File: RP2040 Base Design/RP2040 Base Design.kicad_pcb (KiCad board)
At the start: 2 copper layers, 75 x 23 mm, 27 parts, among them J1 USB_B_Micro, J2 Conn_01x02, J3 RP2040_SWD, U1 RP2040, U2 AMS1117-3.3, U3 W25Q128JVS, Y1 X322512MSB4SI

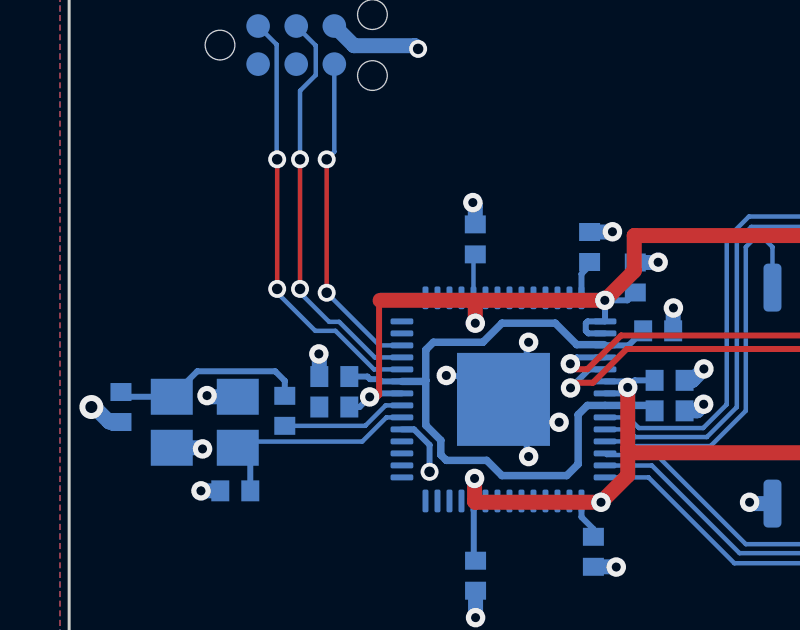
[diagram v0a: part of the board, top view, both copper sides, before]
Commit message: Add 10k pullup resistor to RUN pin for debugging Fixes #2
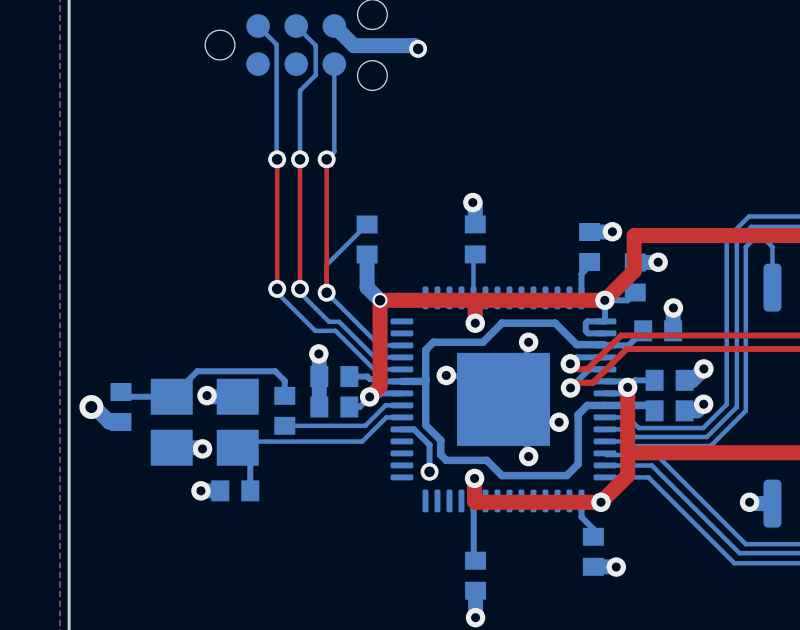
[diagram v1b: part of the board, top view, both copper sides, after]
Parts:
- added R6: 10k, Custom_Footprints:Perfect_0402, B.Cu at (27.0, 26.8)
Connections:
- net /GPIO00 renamed /RP2040/GPIO00
- net /GPIO01 renamed /RP2040/GPIO01
- net /GPIO02 renamed /RP2040/GPIO02
- net /GPIO03 renamed /RP2040/GPIO03
- net /GPIO04 renamed /RP2040/GPIO04
- net /GPIO05 renamed /RP2040/GPIO05
- net /GPIO06 renamed /RP2040/GPIO06
- net /GPIO07 renamed /RP2040/GPIO07
- net /GPIO08 renamed /RP2040/GPIO08
- net /GPIO09 renamed /RP2040/GPIO09
- net /GPIO10 renamed /RP2040/GPIO10
- net /GPIO11 renamed /RP2040/GPIO11
- net /GPIO12 renamed /RP2040/GPIO12
- net /GPIO13 renamed /RP2040/GPIO13
- net /GPIO14 renamed /RP2040/GPIO14
- net /GPIO15 renamed /RP2040/GPIO15
- net /GPIO16 renamed /RP2040/GPIO16
- net /GPIO17 renamed /RP2040/GPIO17
- net /GPIO18 renamed /RP2040/GPIO18
- net /GPIO19 renamed /RP2040/GPIO19
- net /GPIO20 renamed /RP2040/GPIO20
- net /GPIO21 renamed /RP2040/GPIO21
- net /GPIO22 renamed /RP2040/GPIO22
- net /GPIO23 renamed /RP2040/GPIO23
- net /GPIO24 renamed /RP2040/GPIO24
- net /GPIO25 renamed /RP2040/GPIO25
- net /GPIO26 renamed /RP2040/GPIO26
- net /GPIO27 renamed /RP2040/GPIO27
- net /GPIO28 renamed /RP2040/GPIO28
- net /GPIO29 renamed /RP2040/GPIO29
- net /QSPI_SCLK renamed /RP2040/QSPI_SCLK
- net /QSPI_SD0 renamed /RP2040/QSPI_SD0
- net /QSPI_SD1 renamed /RP2040/QSPI_SD1
- net /QSPI_SD2 renamed /RP2040/QSPI_SD2
- net /QSPI_SD3 renamed /RP2040/QSPI_SD3
- net /QSPI_SS renamed /RP2040/QSPI_SS
- net /SWCLK renamed /RP2040/SWCLK
- net /SWD renamed /RP2040/SWD
- net /USB_D+ renamed /RP2040/USB_D+
- net /USB_D- renamed /RP2040/USB_D-
- net /USB_D_R+ renamed /RP2040/USB_D_R+
- net /USB_D_R- renamed /RP2040/USB_D_R-
- net /XIN renamed /RP2040/XIN
- net /XOUT renamed /RP2040/XOUT
- net /XOUT_R renamed /RP2040/XOUT_R
- net /~{RST} renamed /RP2040/~{RST}
- net /~{USB_BOOT} renamed /RP2040/~{USB_BOOT}
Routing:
- net /RP2040/~{RST}: track 11.0 -> 13.8 mm
- net +3V3: track 73.7 -> 75.5 mm, vias 8 -> 9
- net GND: track 25.9 -> 26.9 mm

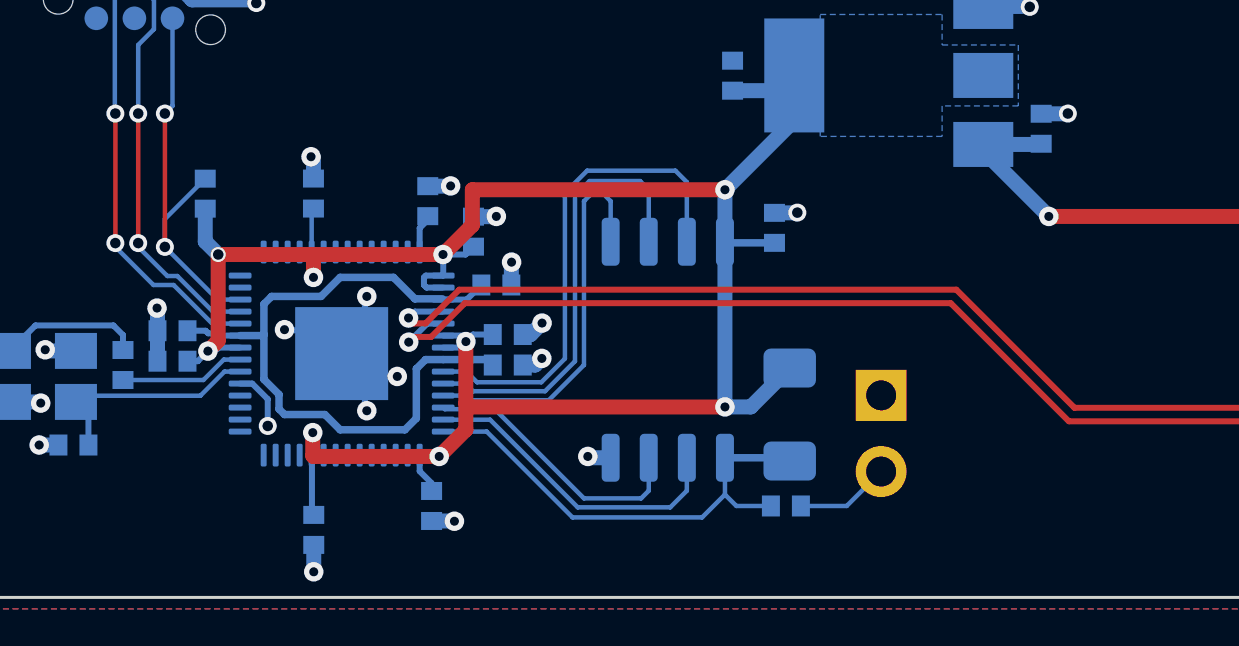
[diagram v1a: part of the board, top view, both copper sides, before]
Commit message: Add default sizes
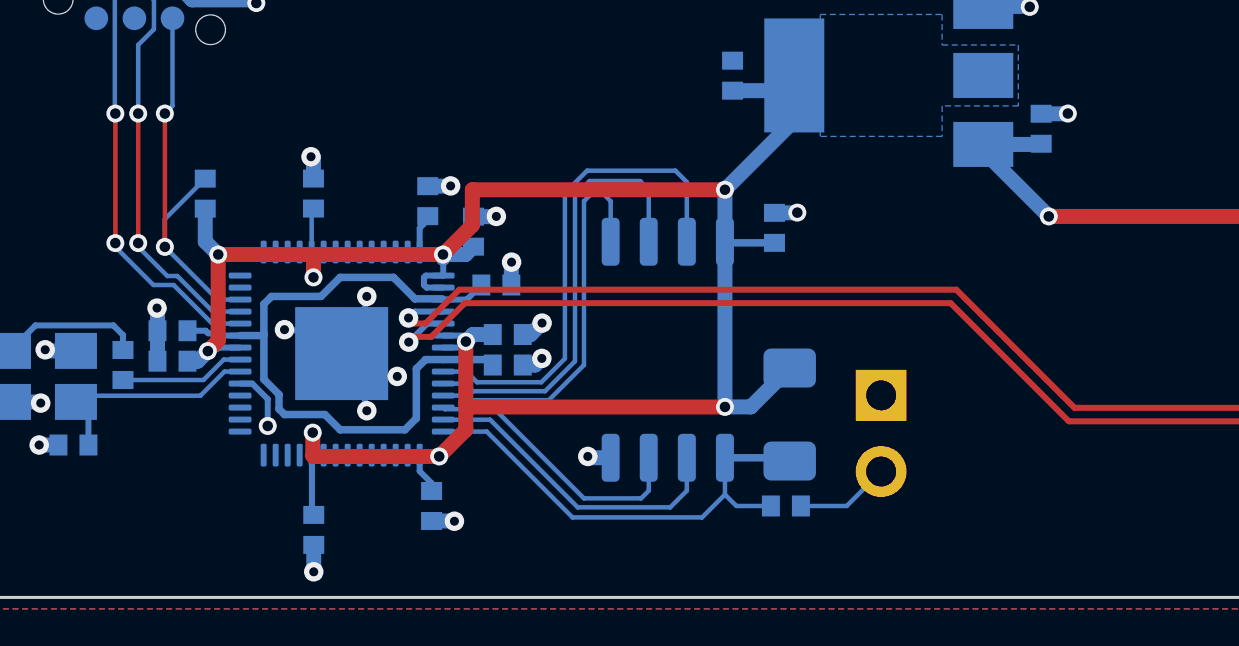
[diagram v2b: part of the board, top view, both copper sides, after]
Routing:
- net +3V3: track 75.5 -> 74.9 mm
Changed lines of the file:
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@@
   (segment (start 89.387 31.75) (end 89.946 32.309) (width 0.5) (layer "F.Cu") (net 4))
   (segment (start 76.835 31.75) (end 89.387 31.75) (width 0.5) (layer "F.Cu") (net 4))
-  (via (at 55.118001 27.558999) (size 0.65) (drill 0.3) (layers "F.Cu" "B.Cu") (net 4))
+  (via (at 55.118001 27.558999) (size 0.6) (drill 0.35) (layers "F.Cu" "B.Cu") (net 4))
   (segment (start 52.934 25.16) (end 54.842 25.16) (width 0.5) (layer "B.Cu") (net 4))
   (segment (start 52.934 25.374998) (end 55.118001 27.558999) (width 0.5) (layer "B.Cu") (net 4))
@@
   (segment (start 34.925 28.829) (end 35.903501 27.850499) (width 0.5) (layer "F.Cu") (net 5))
   (segment (start 35.687 34.671) (end 35.687 33.782) (width 0.5) (layer "F.Cu") (net 5))
-  (segment (start 35.814 33.909) (end 35.687 33.782) (width 0.25) (layer "F.Cu") (net 5))
+  (segment (start 35.814 33.909) (end 35.687 33.782) (width 0.5) (layer "F.Cu") (net 5))
   (segment (start 35.687 33.782) (end 35.687 31.73298) (width 0.5) (layer "F.Cu") (net 5))
   (segment (start 30.607 35.56) (end 34.798 35.56) (width 0.5) (layer "F.Cu") (net 5))
@@
   (segment (start 30.582932 35.535932) (end 30.607 35.56) (width 0.5) (layer "F.Cu") (net 5))
   (segment (start 44.323 33.909) (end 35.814 33.909) (width 0.5) (layer "F.Cu") (net 5))
-  (via (at 30.582932 34.765776) (size 0.65) (drill 0.3) (layers "F.Cu" "B.Cu") (net 5))
-  (via (at 30.607 29.591) (size 0.65) (drill 0.3) (layers "F.Cu" "B.Cu") (net 5))
-  (via (at 27.432 28.829) (size 0.5) (drill 0.35) (layers "F.Cu" "B.Cu") (net 5))
-  (via (at 27.086949 32.04834) (size 0.65) (drill 0.3) (layers "F.Cu" "B.Cu") (net 5))
-  (via (at 44.323 26.67) (size 0.65) (drill 0.3) (layers "F.Cu" "B.Cu") (net 5))
-  (via (at 34.798 35.56) (size 0.65) (drill 0.3) (layers "F.Cu" "B.Cu") (net 5))
-  (via (at 34.925 28.829) (size 0.65) (drill 0.3) (layers "F.Cu" "B.Cu") (net 5))
-  (via (at 44.323 33.909) (size 0.65) (drill 0.3) (layers "F.Cu" "B.Cu") (net 5))
-  (via (at 35.68848 31.7315) (size 0.65) (drill 0.3) (layers "F.Cu" "B.Cu") (net 5))
+  (via (at 30.582932 34.765776) (size 0.6) (drill 0.35) (layers "F.Cu" "B.Cu") (net 5))
+  (via (at 30.607 29.591) (size 0.6) (drill 0.35) (layers "F.Cu" "B.Cu") (net 5))
+  (via (at 27.432 28.829) (size 0.6) (drill 0.35) (layers "F.Cu" "B.Cu") (net 5))
+  (via (at 27.086949 32.04834) (size 0.6) (drill 0.35) (layers "F.Cu" "B.Cu") (net 5))
+  (via (at 44.323 26.67) (size 0.6) (drill 0.35) (layers "F.Cu" "B.Cu") (net 5))
+  (via (at 34.798 35.56) (size 0.6) (drill 0.35) (layers "F.Cu" "B.Cu") (net 5))
+  (via (at 34.925 28.829) (size 0.6) (drill 0.35) (layers "F.Cu" "B.Cu") (net 5))
+  (via (at 44.323 33.909) (size 0.6) (drill 0.35) (layers "F.Cu" "B.Cu") (net 5))
+  (via (at 35.68848 31.7315) (size 0.6) (drill 0.35) (layers "F.Cu" "B.Cu") (net 5))
   (segment (start 45.974 28.44) (end 44.359 28.44) (width 0.25) (layer "B.Cu") (net 5))
-  (segment (start 34.754 35.516) (end 34.798 35.56) (width 0.2) (layer "B.Cu") (net 5))
+  (segment (start 34.754 35.516) (end 34.798 35.56) (width 0.5) (layer "B.Cu") (net 5))
   (segment (start 45.186 33.909) (end 44.323 33.909) (width 0.5) (layer "B.Cu") (net 5))
-  (segment (start 34.925 28.956) (end 34.925 28.829) (width 0.2) (layer "B.Cu") (net 5))
-  (segment (start 26.408 32.385) (end 26.750289 32.385) (width 0.2) (layer "B.Cu") (net 5))
+  (segment (start 34.925 28.956) (end 34.925 28.829) (width 0.5) (layer "B.Cu") (net 5))
+  (segment (start 26.408 32.385) (end 26.750289 32.385) (width 0.5) (layer "B.Cu") (net 5))
   (segment (start 34.9318 29.531) (end 34.35 29.531) (width 0.2) (layer "B.Cu") (net 5))
   (segment (start 34.1468 35.516) (end 34.754 35.516) (width 0.2) (layer "B.Cu") (net 5))
-  (segment (start 36.584 31.496) (end 35.92398 31.496) (width 0.2) (layer "B.Cu") (net 5))
+  (segment (start 36.584 31.496) (end 35.92398 31.496) (width 0.5) (layer "B.Cu") (net 5))
   (segment (start 27.45196 31.931) (end 27.400668 31.982292) (width 0.2) (layer "B.Cu") (net 5))
   (segment (start 34.1468 35.516) (end 34.1468 36.0518) (width 0.2) (layer "B.Cu") (net 5))
-  (segment (start 35.595 31.531) (end 35.68848 31.62448) (width 0.2) (layer "B.Cu") (net 5))
   (segment (start 44.323 26.67) (end 44.323 28.404) (width 0.5) (layer "B.Cu") (net 5))
-  (segment (start 30.5468 34.801908) (end 30.582932 34.765776) (width 0.2) (layer "B.Cu") (net 5))
-  (segment (start 35.92398 31.496) (end 35.68848 31.7315) (width 0.2) (layer "B.Cu") (net 5))
-  (segment (start 35.48898 31.931) (end 35.68848 31.7315) (width 0.2) (layer "B.Cu") (net 5))
+  (segment (start 30.5468 34.801908) (end 30.582932 34.765776) (width 0.5) (layer "B.Cu") (net 5))
+  (segment (start 35.92398 31.496) (end 35.68848 31.7315) (width 0.5) (layer "B.Cu") (net 5))
   (segment (start 46.482 32.613) (end 45.186 33.909) (width 0.5) (layer "B.Cu") (net 5))
-  (segment (start 35.68848 31.62448) (end 35.68848 31.7315) (width 0.2) (layer "B.Cu") (net 5))
   (segment (start 46.126 23.368) (end 44.577 23.368) (width 0.5) (layer "B.Cu") (net 5))
   (segment (start 34.376 29.931) (end 34.9318 29.931) (width 0.2) (layer "B.Cu") (net 5))
@@
   (segment (start 34.544 36.449) (end 34.544 36.711) (width 0.2) (layer "B.Cu") (net 5))
   (segment (start 34.1468 28.746) (end 34.1468 27.9482) (width 0.2) (layer "B.Cu") (net 5))
-  (segment (start 34.925 28.829) (end 35.679 28.829) (width 0.2) (layer "B.Cu") (net 5))
+  (segment (start 34.925 28.829) (end 35.679 28.829) (width 0.5) (layer "B.Cu") (net 5))
   (segment (start 34.9318 31.931) (end 35.48898 31.931) (width 0.2) (layer "B.Cu") (net 5))
   (segment (start 30.5468 28.746) (end 30.5468 27.3572) (width 0.15) (layer "B.Cu") (net 5))
@@
   (segment (start 27 28.397) (end 27.432 28.829) (width 0.5) (layer "B.Cu") (net 5))
   (segment (start 34.29 29.591) (end 34.29 29.845) (width 0.2) (layer "B.Cu") (net 5))
-  (segment (start 30.5468 29.5308) (end 30.607 29.591) (width 0.2) (layer "B.Cu") (net 5))
   (segment (start 34.1468 28.746) (end 34.715 28.746) (width 0.2) (layer "B.Cu") (net 5))
-  (segment (start 26.750289 32.385) (end 27.086949 32.04834) (width 0.2) (layer "B.Cu") (net 5))
+  (segment (start 26.750289 32.385) (end 27.086949 32.04834) (width 0.5) (layer "B.Cu") (net 5))
   (segment (start 27 27.3) (end 27 28.397) (width 0.5) (layer "B.Cu") (net 5))
   (segment (start 34.715 28.746) (end 34.9318 28.9628) (width 0.2) (layer "B.Cu") (net 5))
-  (segment (start 35.679 28.829) (end 35.941 28.567) (width 0.2) (layer "B.Cu") (net 5))
+  (segment (start 35.679 28.829) (end 35.941 28.567) (width 0.5) (layer "B.Cu") (net 5))
   (segment (start 46.634 24.359) (end 44.323 26.67) (width 0.5) (layer "B.Cu") (net 5))
   (segment (start 34.1468 27.9482) (end 34.544 27.551) (width 0.2) (layer "B.Cu") (net 5))
